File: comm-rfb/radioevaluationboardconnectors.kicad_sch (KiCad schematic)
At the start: 4 parts, among them J2 TFM-110-02-SM-D-A-K-TR, J3 TFM-110-02-SM-D-A-K-TR

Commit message: comm-rfb: reduce number of sheets in schematic
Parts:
- J2, J3: value TFM-110-02-SM-D-A-K-TR -> (none); footprint SAMTEC_TFM-110-02-SM-D-A-K-TR -> (none)
- J4, J5: renamed from J?; value TFM-110-02-SM-D-A-K-TR -> (none); footprint SAMTEC_TFM-110-02-SM-D-A-K-TR -> (none)
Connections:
- no-connect marks 30 -> 60

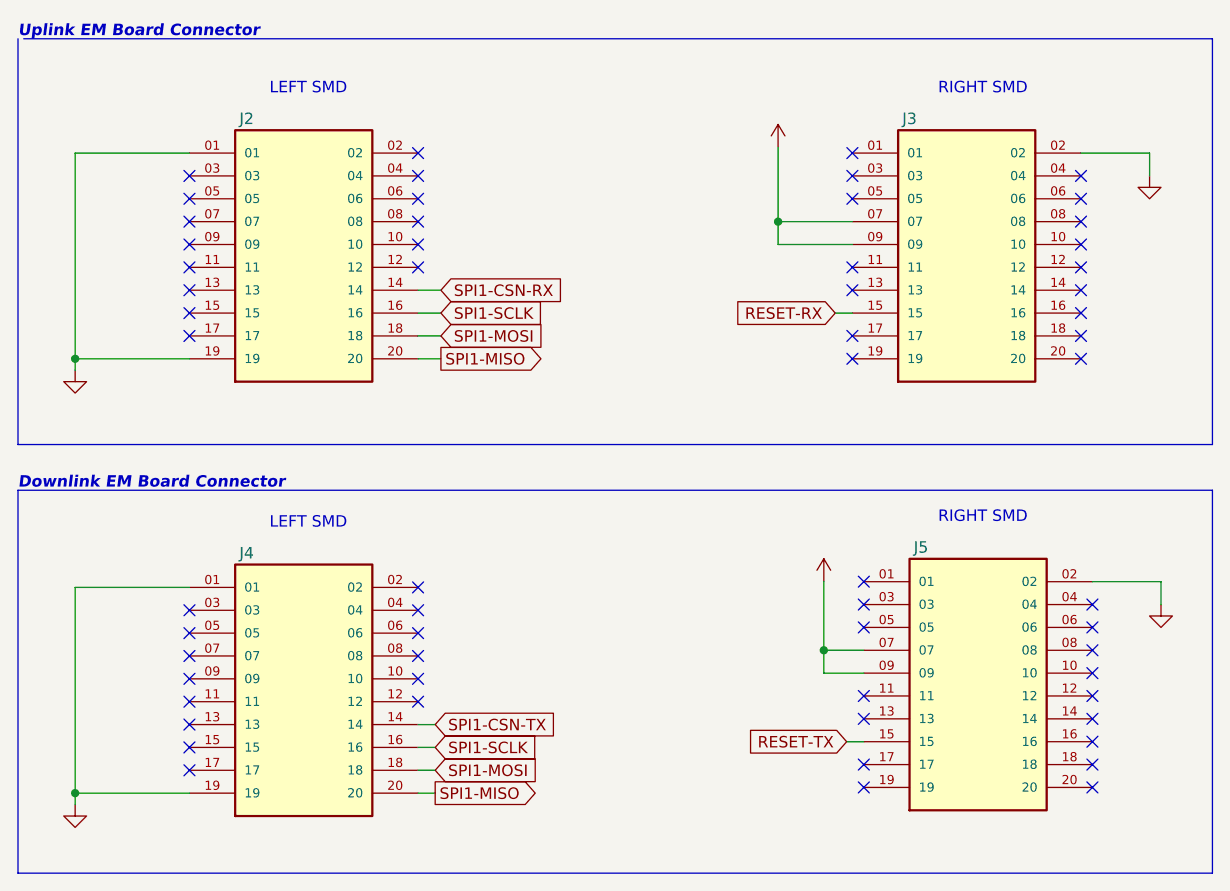
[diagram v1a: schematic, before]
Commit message: comm-rfb: reformat for rebase
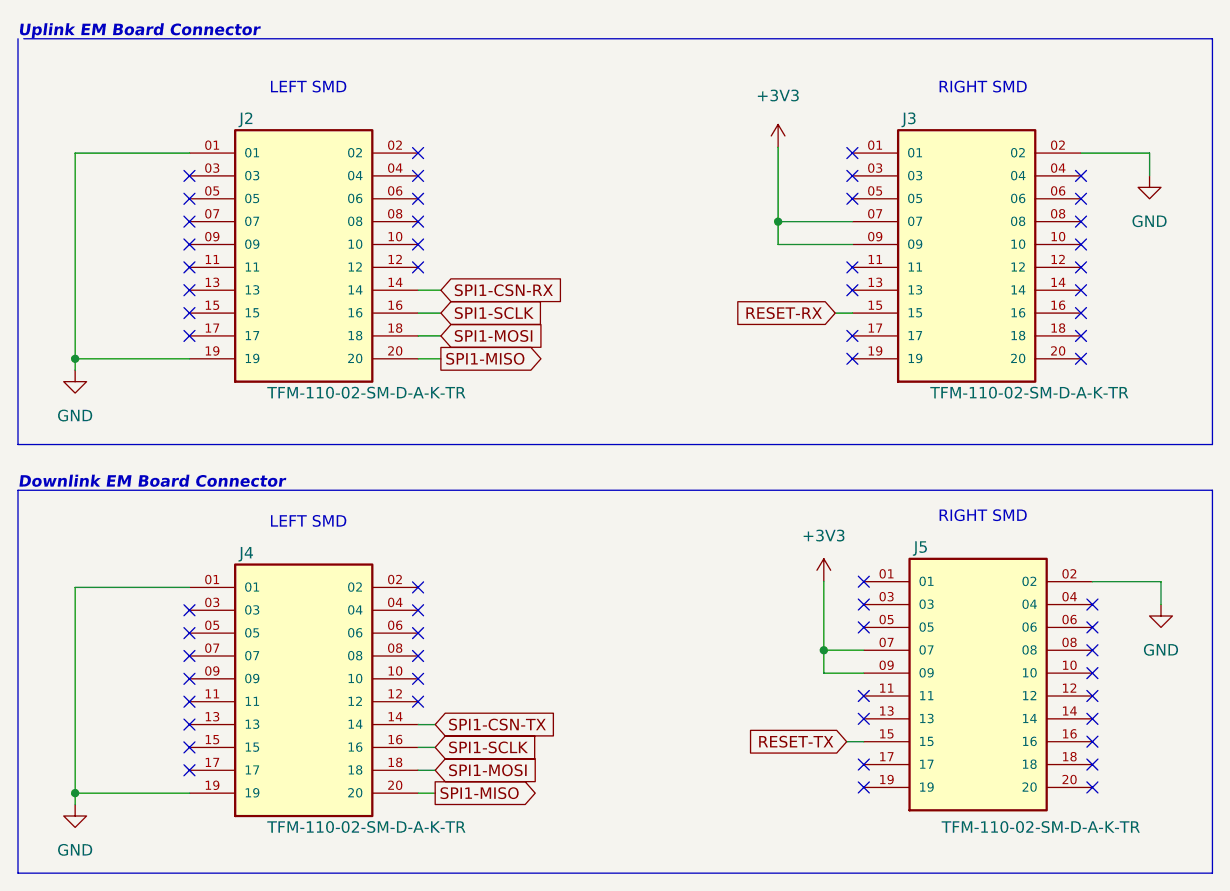
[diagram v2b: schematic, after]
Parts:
- J2, J3, J4, J5: value (none) -> TFM-110-02-SM-D-A-K-TR; footprint (none) -> SAMTEC_TFM-110-02-SM-D-A-K-TR
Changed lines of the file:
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@@
     (in_bom yes) (on_board yes)
     (property "Reference" "J2" (id 0) (at 106.045 48.895 0))
-    (property "Value" "" (id 1) (at 119.38 79.375 0))
-    (property "Footprint" "" (id 2) (at 112.395 65.405 0)
+    (property "Value" "TFM-110-02-SM-D-A-K-TR" (id 1) (at 119.38 79.375 0))
+    (property "Footprint" "SAMTEC_TFM-110-02-SM-D-A-K-TR" (id 2) (at 112.395 65.405 0)
       (effects (font (size 1.27 1.27)) (justify bottom) hide)
     )
@@
     (in_bom yes) (on_board yes)
     (property "Reference" "J4" (id 0) (at 106.045 97.155 0))
-    (property "Value" "" (id 1) (at 119.38 127.635 0))
-    (property "Footprint" "" (id 2) (at 112.395 113.665 0)
+    (property "Value" "TFM-110-02-SM-D-A-K-TR" (id 1) (at 119.38 127.635 0))
+    (property "Footprint" "SAMTEC_TFM-110-02-SM-D-A-K-TR" (id 2) (at 112.395 113.665 0)
       (effects (font (size 1.27 1.27)) (justify bottom) hide)
     )
@@
       (effects (font (size 1.27 1.27)) hide)
     )
-    (property "Value" "" (id 1) (at 206.375 60.325 0))
+    (property "Value" "GND" (id 1) (at 206.375 60.325 0))
     (property "Footprint" "" (id 2) (at 206.375 55.245 0)
       (effects (font (size 1.27 1.27)) hide)
@@
       (effects (font (size 1.27 1.27)) hide)
     )
-    (property "Value" "" (id 1) (at 165.1 46.355 0))
+    (property "Value" "+3V3" (id 1) (at 165.1 46.355 0))
     (property "Footprint" "" (id 2) (at 165.1 52.07 0)
       (effects (font (size 1.27 1.27)) hide)
@@
     (in_bom yes) (on_board yes)
     (property "Reference" "J5" (id 0) (at 180.975 96.52 0))
-    (property "Value" "" (id 1) (at 194.31 127.635 0))
-    (property "Footprint" "" (id 2) (at 187.325 113.03 0)
+    (property "Value" "TFM-110-02-SM-D-A-K-TR" (id 1) (at 194.31 127.635 0))
+    (property "Footprint" "SAMTEC_TFM-110-02-SM-D-A-K-TR" (id 2) (at 187.325 113.03 0)
       (effects (font (size 1.27 1.27)) (justify bottom) hide)
     )
@@
       (effects (font (size 1.27 1.27)) hide)
     )
-    (property "Value" "" (id 1) (at 86.995 130.175 0))
+    (property "Value" "GND" (id 1) (at 86.995 130.175 0))
     (property "Footprint" "" (id 2) (at 86.995 125.095 0)
       (effects (font (size 1.27 1.27)) hide)
@@
       (effects (font (size 1.27 1.27)) hide)
     )
-    (property "Value" "" (id 1) (at 170.18 95.25 0))
+    (property "Value" "+3V3" (id 1) (at 170.18 95.25 0))
     (property "Footprint" "" (id 2) (at 170.18 100.33 0)
       (effects (font (size 1.27 1.27)) hide)
@@
       (effects (font (size 1.27 1.27)) hide)
     )
-    (property "Value" "" (id 1) (at 207.645 107.95 0))
+    (property "Value" "GND" (id 1) (at 207.645 107.95 0))
     (property "Footprint" "" (id 2) (at 207.645 102.87 0)
       (effects (font (size 1.27 1.27)) hide)
@@
       (effects (font (size 1.27 1.27)) hide)
     )
-    (property "Value" "" (id 1) (at 86.995 81.915 0))
+    (property "Value" "GND" (id 1) (at 86.995 81.915 0))
     (property "Footprint" "" (id 2) (at 86.995 76.835 0)
       (effects (font (size 1.27 1.27)) hide)
@@
     (in_bom yes) (on_board yes)
     (property "Reference" "J3" (id 0) (at 179.705 48.895 0))
-    (property "Value" "" (id 1) (at 193.04 79.375 0))
-    (property "Footprint" "" (id 2) (at 186.055 65.405 0)
-      (effects (font (size 1.27 1.27)) (justify bottom) hide)
-    )
+    (property "Value" "TFM-110-02-SM-D-A-K-TR" (id 1) (at 193.04 79.375 0))
+    (property "Footprint" "SAMTEC_TFM-110-02-SM-D-A-K-TR" (id 2) (at 186.055 65.405 0)
+      (effects (font (size 1.27 1.27)) (justify bottom) hide)
+    )
